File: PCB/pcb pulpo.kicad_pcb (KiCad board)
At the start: 2 copper layers, 37 parts, among them J1 fan1, J2 Entrada 12V, J3 fan2, J4 fan3, J5 fan4, J6 fan5, J7 fan6, J8 fan7, J9 fan8, Q1 IRF540N, Q2 IRF540N, Q3 IRF540N, Q4 IRF540N, Q5 IRF540N, Q6 IRF540N, Q7 IRF540N, Q8 IRF540N, U1 Teensy3.0, U2 LM7805_TO220

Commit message: Boceto PCB
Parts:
- added D10: DIODE, Diode_THT:D_DO-34_SOD68_P10.16mm_Horizontal, F.Cu at (105.7, 32.2)
- added D9: DIODE, Diode_THT:D_DO-34_SOD68_P10.16mm_Horizontal, F.Cu at (105.7, 47.5)
- added J10: fan8, TerminalBlock:TerminalBlock_bornier-2_P5.08mm, F.Cu at (112.7, 44.9)
- added J11: fan8, TerminalBlock:TerminalBlock_bornier-2_P5.08mm, F.Cu at (112.7, 29.6)
- added J12: izq, Connector_PinSocket_2.54mm:PinSocket_1x14_P2.54mm_Vertical, F.Cu at (59.1, 52.1)
- added J13: dcha, Connector_PinSocket_2.54mm:PinSocket_1x14_P2.54mm_Vertical, F.Cu at (80.6, 52.1)
- added J14: inf, Connector_PinSocket_2.54mm:PinSocket_1x05_P2.54mm_Vertical, F.Cu at (64.8, 88.3)
- added Q10: IRF540N, Package_TO_SOT_THT:TO-220-3_Vertical, F.Cu at (96.2, 29.6)
- added Q9: IRF540N, Package_TO_SOT_THT:TO-220-3_Vertical, F.Cu at (96.2, 44.9)
- added R10: R, Resistor_THT:R_Axial_DIN0207_L6.3mm_D2.5mm_P10.16mm_Horizontal, F.Cu at (101.3, 22.0)
- added R9: R, Resistor_THT:R_Axial_DIN0207_L6.3mm_D2.5mm_P10.16mm_Horizontal, F.Cu at (101.3, 37.3)
- moved J8 101.6 mm to (112.7, 75.5), turned to 90 degrees
- moved J4 94.0 mm to (26.7, 55.1), turned to 270 degrees
- moved J7 92.3 mm to (112.7, 90.9), turned to 90 degrees
- moved J5 88.3 mm to (26.7, 70.4), turned to 270 degrees
- moved D7 86.6 mm to (105.7, 78.1), turned to 90 degrees
- moved J9 85.5 mm to (112.7, 60.1), turned to 90 degrees
- moved D3 82.0 mm to (33.7, 52.6), turned to 270 degrees
- moved R7 79.6 mm to (101.3, 67.9), turned to 270 degrees
- moved D6 79.3 mm to (105.7, 93.1), turned to 90 degrees
- moved D4 76.3 mm to (33.7, 67.7), turned to 270 degrees
- moved J3 75.2 mm to (26.7, 39.8), turned to 270 degrees
- moved D8 71.1 mm to (105.7, 62.6), turned to 90 degrees
- moved R6 69.3 mm to (101.3, 83.2), turned to 270 degrees
- moved R8 68.5 mm to (101.3, 52.5), turned to 270 degrees
- moved D2 66.4 mm to (33.7, 37.3), turned to 270 degrees
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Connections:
- U1 pad 11: Net-(U1-Pad11) -> pin5
- U1 pad 12: Net-(U1-Pad12) -> pin6
- U1 pad 28: Net-(U1-Pad28) -> pin7
- U1 pad 29: Net-(U1-Pad29) -> pin8
- U1 pad 30: Net-(U1-Pad30) -> pin9
- U1 pad 31: Net-(U1-Pad31) -> pin10
- U1 pad 39: Net-(U1-Pad39) -> GND
- U1 pad 5: Net-(U1-Pad5) -> pin1
- U1 pad 6: Net-(U1-Pad6) -> pin2
- U1 pad 7: Net-(U1-Pad7) -> pin3
- U1 pad 8: Net-(U1-Pad8) -> pin4
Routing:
- net +12V: track 567.7 -> 460.0 mm
- net pin6: track 7.05 -> 58.6 mm
- net GND: track 294.7 -> 323.4 mm
- net Net-(D10-Pad1): track 0.00 -> 19.8 mm
- net Net-(D9-Pad1): track 0.00 -> 19.7 mm
- net Net-(C2-Pad1): track 8.15 -> 22.4 mm
- net pin9: track 0.00 -> 9.34 mm
- net pin10: track 0.00 -> 9.31 mm
- net Net-(J14-Pad4): track 0.00 -> 3.17 mm
- net Net-(J14-Pad2): track 0.00 -> 3.17 mm
- net Net-(J14-Pad1): track 0.00 -> 3.17 mm
- net Net-(J13-Pad9): track 0.00 -> 3.17 mm
- net Net-(J13-Pad8): track 0.00 -> 3.17 mm
- net Net-(J13-Pad7): track 0.00 -> 3.17 mm
- net Net-(J13-Pad2): track 0.00 -> 3.17 mm
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
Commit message: placa terminada
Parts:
- J2: footprint TerminalBlock:TerminalBlock_bornier-2_P5.08mm -> teensy:conector pablo pulpo hinchoshwi
- moved J7 10.0 mm to (106.2, 83.2)
- moved Q6 10.0 mm to (89.7, 83.2)
- moved D6 10.0 mm to (99.3, 85.5)
- moved R6 10.0 mm to (94.8, 75.6)
- moved D7 8.64 mm to (99.3, 72.4)
- moved R7 8.64 mm to (94.8, 62.2)
- moved J8 8.64 mm to (106.2, 69.8)
- moved Q7 8.64 mm to (89.7, 69.8)
- moved D5 8.10 mm to (35.6, 75.0)
- moved Q5 8.10 mm to (45.2, 77.9)
- moved R5 8.10 mm to (40.1, 85.5)
- moved J6 8.10 mm to (28.6, 77.9)
- moved D8 7.51 mm to (99.3, 58.8)
- moved J9 7.51 mm to (106.2, 56.3)
- moved R8 7.51 mm to (94.8, 48.7)
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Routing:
- net GND: track 323.4 -> 6.35 mm
- net +12V: track 460.0 -> 339.7 mm
- net pin6: track 58.6 -> 15.9 mm, vias 0 -> 1
- net pin7: track 9.31 -> 15.9 mm, vias 0 -> 1
- net pin1: track 9.31 -> 15.9 mm, vias 0 -> 1
- net pin2: track 9.31 -> 15.8 mm, vias 0 -> 1
- net pin3: track 9.31 -> 15.8 mm, vias 0 -> 1
- net pin10: track 9.31 -> 15.8 mm, vias 0 -> 1
- net pin9: track 9.34 -> 15.8 mm, vias 0 -> 1
- net pin8: track 9.31 -> 15.8 mm, vias 0 -> 1
- net pin4: track 9.31 -> 15.7 mm, vias 0 -> 1
- net pin5: track 9.31 -> 15.7 mm, vias 0 -> 1
- net Net-(C2-Pad1): track 22.4 -> 18.9 mm
- added copper zone on B.Cu, net GND
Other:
- board outline added: 90.4 x 74.7 mm

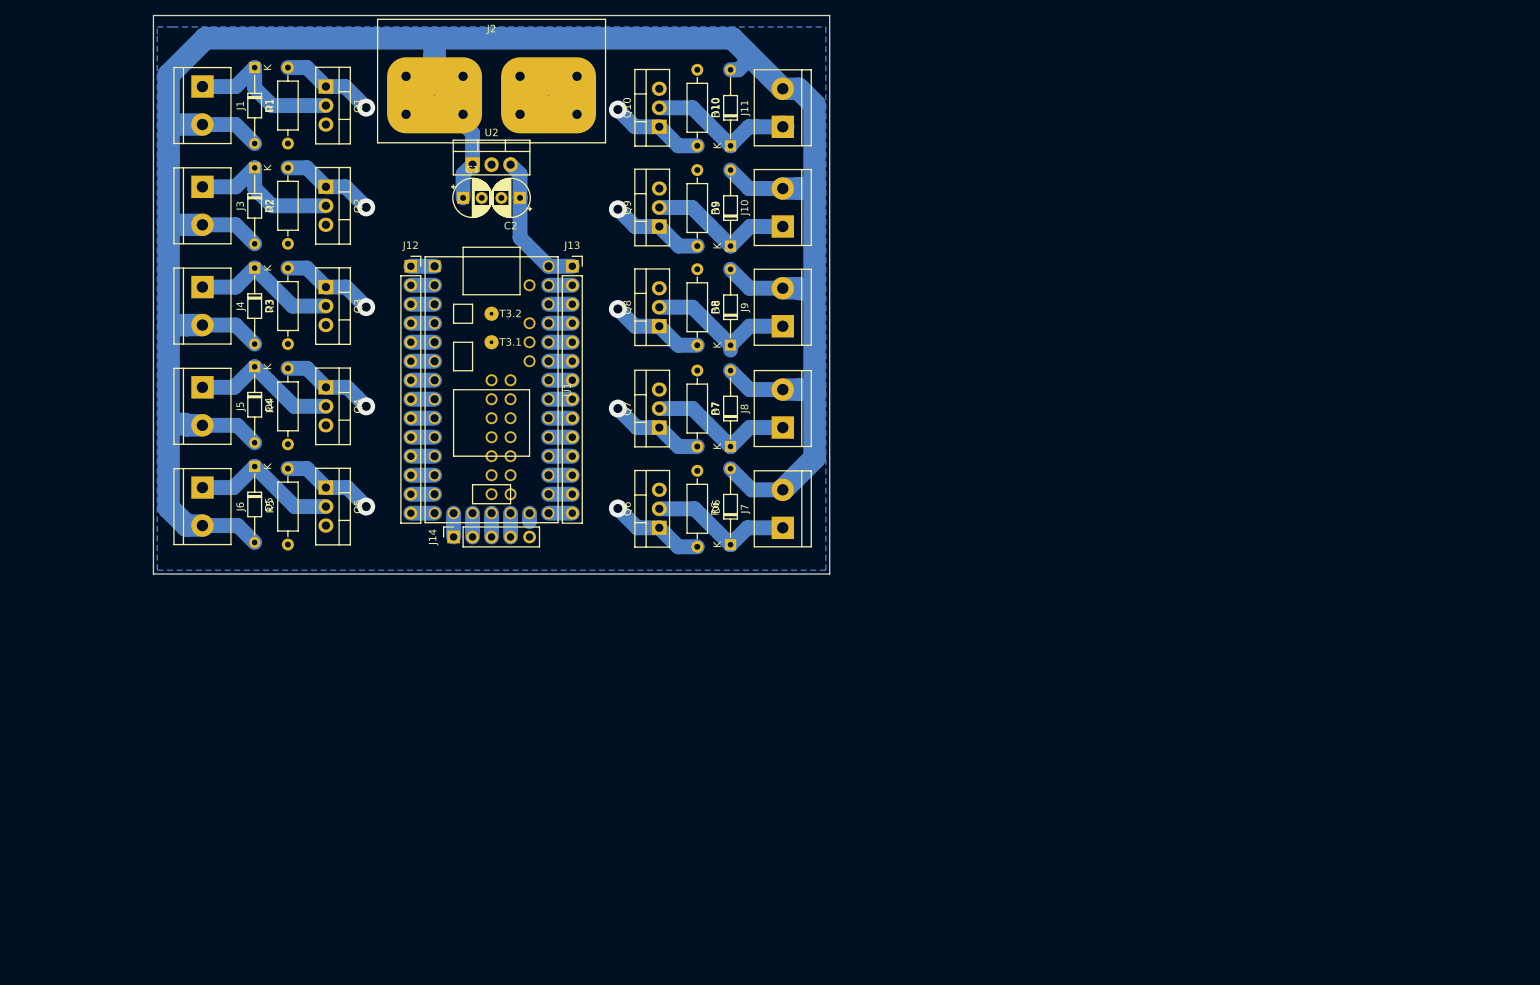
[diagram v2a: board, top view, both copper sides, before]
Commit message: añadidos leds a la placa y junta para la cabeza
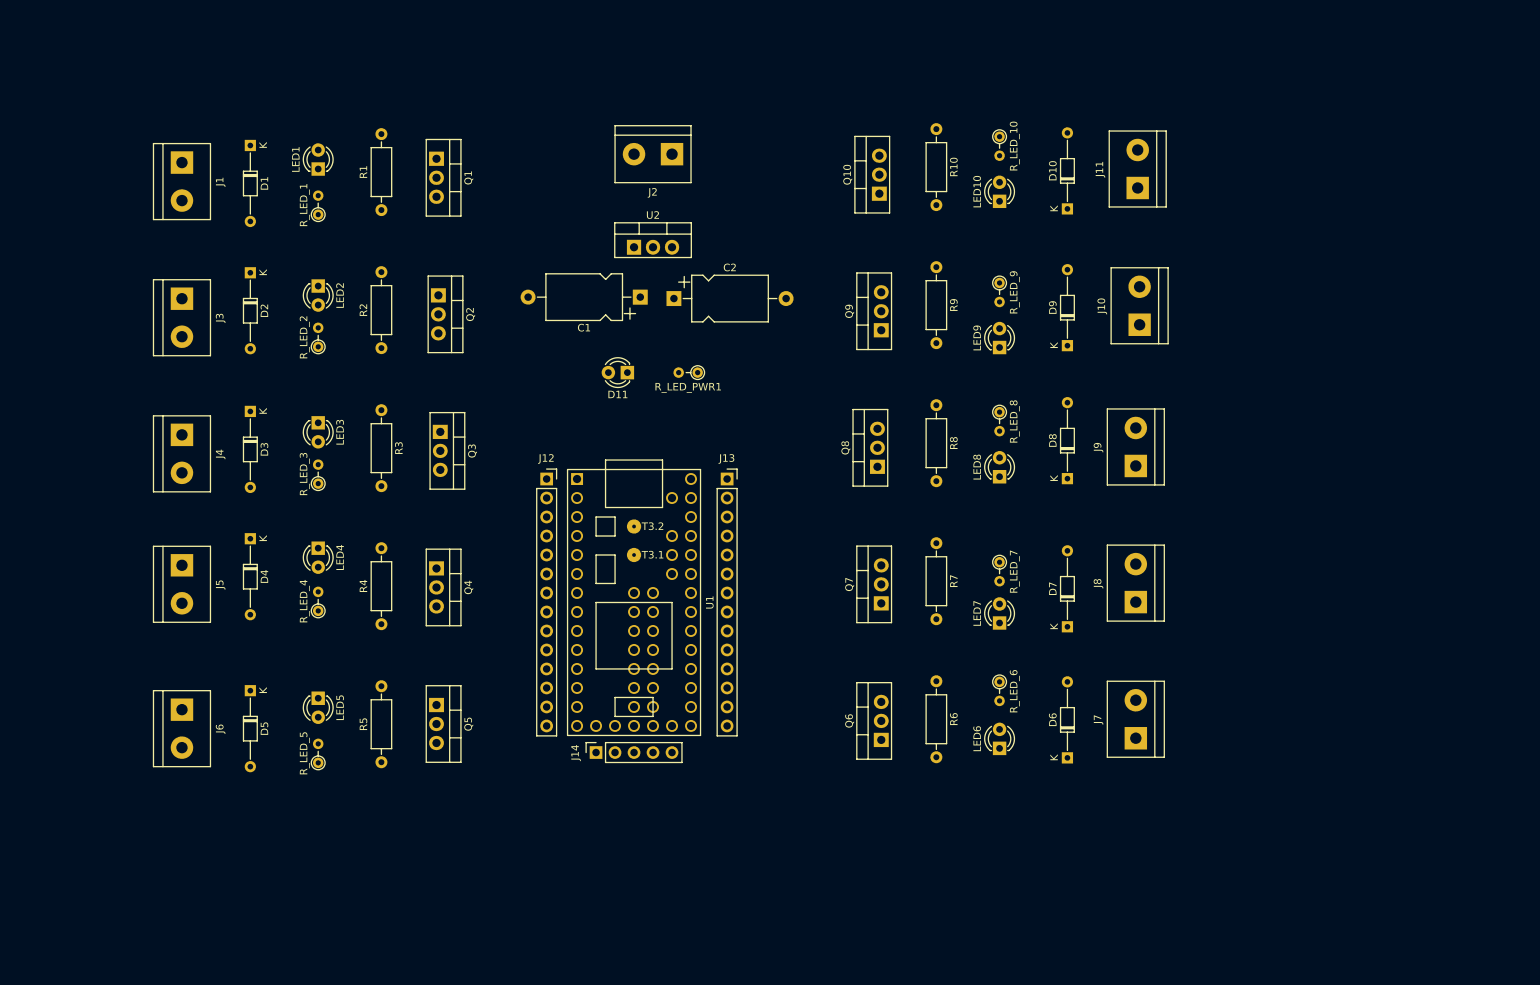
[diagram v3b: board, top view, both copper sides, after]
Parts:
- added D11: LED, LED_THT:LED_D3.0mm, F.Cu at (85.5, 62.5)
- added LED1: LED, LED_THT:LED_D3.0mm, F.Cu at (44.1, 35.3)
- added LED10: LED, LED_THT:LED_D3.0mm, F.Cu at (135.2, 39.6)
- added LED2: LED, LED_THT:LED_D3.0mm, F.Cu at (44.1, 50.9)
- added LED3: LED, LED_THT:LED_D3.0mm, F.Cu at (44.1, 69.2)
- added LED4: LED, LED_THT:LED_D3.0mm, F.Cu at (44.1, 86.0)
- added LED5: LED, LED_THT:LED_D3.0mm, F.Cu at (44.1, 106.0)
- added LED6: LED, LED_THT:LED_D3.0mm, F.Cu at (135.2, 112.7)
- added LED7: LED, LED_THT:LED_D3.0mm, F.Cu at (135.2, 96.0)
- added LED8: LED, LED_THT:LED_D3.0mm, F.Cu at (135.2, 76.4)
- added LED9: LED, LED_THT:LED_D3.0mm, F.Cu at (135.2, 59.1)
- added R_LED_1: R_LED, Resistor_THT:R_Axial_DIN0204_L3.6mm_D1.6mm_P2.54mm_Vertical, F.Cu at (44.1, 41.4)
- added R_LED_10: R_LED, Resistor_THT:R_Axial_DIN0204_L3.6mm_D1.6mm_P2.54mm_Vertical, F.Cu at (135.2, 30.9)
- added R_LED_2: R_LED, Resistor_THT:R_Axial_DIN0204_L3.6mm_D1.6mm_P2.54mm_Vertical, F.Cu at (44.1, 59.0)
- added R_LED_3: R_LED, Resistor_THT:R_Axial_DIN0204_L3.6mm_D1.6mm_P2.54mm_Vertical, F.Cu at (44.1, 77.3)
- added R_LED_4: R_LED, Resistor_THT:R_Axial_DIN0204_L3.6mm_D1.6mm_P2.54mm_Vertical, F.Cu at (44.1, 94.3)
- added R_LED_5: R_LED, Resistor_THT:R_Axial_DIN0204_L3.6mm_D1.6mm_P2.54mm_Vertical, F.Cu at (44.1, 114.7)
- added R_LED_6: R_LED, Resistor_THT:R_Axial_DIN0204_L3.6mm_D1.6mm_P2.54mm_Vertical, F.Cu at (135.2, 103.8)
- added R_LED_7: R_LED, Resistor_THT:R_Axial_DIN0204_L3.6mm_D1.6mm_P2.54mm_Vertical, F.Cu at (135.2, 87.8)
- added R_LED_8: R_LED, Resistor_THT:R_Axial_DIN0204_L3.6mm_D1.6mm_P2.54mm_Vertical, F.Cu at (135.2, 67.8)
- added R_LED_9: R_LED, Resistor_THT:R_Axial_DIN0204_L3.6mm_D1.6mm_P2.54mm_Vertical, F.Cu at (135.2, 50.5)
- added R_LED_PWR1: R_Small, Resistor_THT:R_Axial_DIN0204_L3.6mm_D1.6mm_P2.54mm_Vertical, F.Cu at (94.9, 62.5)
- C1, C2: footprint Capacitor_THT:CP_Radial_D5.0mm_P2.50mm -> Capacitor_THT:CP_Axial_L10.0mm_D6.0mm_P15.00mm_Horizontal
- J2: footprint teensy:conector pablo pulpo hinchoshwi -> TerminalBlock:TerminalBlock_bornier-2_P5.08mm
- moved J7 55.0 mm to (153.5, 111.4)
- moved D6 53.3 mm to (144.3, 114.0)
- moved J8 52.7 mm to (153.5, 93.2)
- moved D7 51.1 mm to (144.3, 96.5)
- moved J9 50.8 mm to (153.5, 75.0)
- moved J10 49.5 mm to (154.0, 56.1)
- moved D8 48.5 mm to (144.3, 76.7)
- moved J11 48.2 mm to (153.7, 37.8)
- moved D9 47.0 mm to (144.3, 58.9)
- moved D10 45.8 mm to (144.3, 40.6)
- moved R6 42.6 mm to (126.8, 103.7)
- moved Q6 41.1 mm to (119.4, 111.6)
- moved R7 39.4 mm to (126.8, 85.3)
- moved Q7 37.9 mm to (119.4, 93.3)
- moved R8 36.8 mm to (126.8, 66.8)
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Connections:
- U1 pad 19: Net-(U1-Pad19) -> Net-(J14-Pad5)
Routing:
- net +12V: track 339.7 -> 0.00 mm
- net Net-(D2-Pad1): track 21.3 -> 0.00 mm
- net Net-(D1-Pad1): track 21.3 -> 0.00 mm
- net Net-(D8-Pad1): track 20.3 -> 0.00 mm
- net Net-(D5-Pad1): track 19.9 -> 0.00 mm
- net Net-(D4-Pad1): track 19.8 -> 0.00 mm
- net Net-(D10-Pad1): track 19.8 -> 0.00 mm
- net Net-(D9-Pad1): track 19.7 -> 0.00 mm
- net Net-(D3-Pad1): track 19.7 -> 0.00 mm
- net Net-(D7-Pad1): track 19.7 -> 0.00 mm
- net Net-(D6-Pad1): track 19.4 -> 0.00 mm
- net Net-(C2-Pad1): track 18.9 -> 0.00 mm
- net pin6: track 15.9 -> 0.00 mm, vias 1 -> 0
- net pin7: track 15.9 -> 0.00 mm, vias 1 -> 0
- net pin1: track 15.9 -> 0.00 mm, vias 1 -> 0
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- removed copper zone on B.Cu, net GND
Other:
- board outline removed
